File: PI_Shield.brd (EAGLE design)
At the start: 153.7 x 84.8 mm, 64 parts, among them Q1 220mA/50V/3.5Ω, Q3 220mA/50V/3.5Ω, Q4 220mA/50V/3.5Ω, Q5 2.5A/30V/105mΩ, U1 MAX1136EUA-T, U2 AZ1117EH-3.3TRG1, Y1 ECS-80-S-4X

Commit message: Update PI_Shield.brd
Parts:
- moved C11 191.3 mm to (49.5, -21.6)
- moved C12 191.3 mm to (45.7, -21.6)
- moved C13 191.3 mm to (41.9, -21.6)
- moved C3 191.3 mm to (72.4, -21.6)
- moved C4 191.3 mm to (68.6, -21.6)
- moved C5 191.3 mm to (64.8, -21.6)
- moved C6 191.3 mm to (61.0, -21.6)
- moved C8 191.3 mm to (57.1, -21.6)
- moved C9 191.3 mm to (53.3, -21.6)
- moved D1 191.3 mm to (77.5, -21.6)
- moved D2 191.3 mm to (68.6, -17.8)
- moved D4 191.3 mm to (64.8, -17.8)
- moved R1 191.3 mm to (38.1, -21.6)
- moved R10 191.3 mm to (99.1, -16.5)
- moved R11 191.3 mm to (82.5, -21.6)
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
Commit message: Update PI_Shield.brd
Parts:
- moved C4 13.1 mm to (74.9, -10.2)
- moved C5 13.1 mm to (71.1, -10.2)
- moved D2 13.1 mm to (74.9, -6.35)
- moved D4 13.1 mm to (71.1, -6.35)
- moved R11 13.1 mm to (88.9, -10.2)
- moved R13 13.1 mm to (97.8, -5.08)
- moved R14 13.1 mm to (94.0, -5.08)
- moved R15 13.1 mm to (90.2, -5.08)
- moved R4 13.1 mm to (128.3, -5.08)
- moved R6 13.1 mm to (120.7, -5.08)
- moved R7 13.1 mm to (116.8, -5.08)
- moved C11 13.1 mm to (55.9, -10.2)
- moved C12 13.1 mm to (52.1, -10.2)
- moved C13 13.1 mm to (48.3, -10.2)
- moved C6 13.1 mm to (67.3, -10.2)
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
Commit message: Update PI_Shield.brd
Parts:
- moved R4 90.8 mm to (43.2, 26.7), turned to 90 degrees
- moved R5 83.7 mm to (47.0, 26.7), turned to 90 degrees
- moved C12 83.0 mm to (43.2, 72.4)
- moved 0 76.3 mm to (68.6, 62.2)
- moved R10 75.5 mm to (49.5, 45.7), turned to 90 degrees
- moved R12 73.5 mm to (31.8, 17.8), turned to 90 degrees
- moved C11 72.3 mm to (33.0, 58.4)
- moved R11 70.3 mm to (68.6, 57.1)
- moved R14 70.1 mm to (36.8, 35.6), turned to 270 degrees
- moved R15 69.1 mm to (31.8, 31.8), turned to 180 degrees
- moved C3 68.7 mm to (49.5, 52.1), turned to 270 degrees
- moved R13 67.1 mm to (36.8, 22.9), turned to 270 degrees
- moved R8 63.2 mm to (52.1, 11.4), turned to 90 degrees
- moved R2 62.0 mm to (64.8, 47.0), turned to 90 degrees
- moved D1 60.4 mm to (61.0, 45.7), turned to 270 degrees
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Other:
- board size 153.7 x 84.8 mm -> 85.1 x 84.8 mm

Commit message: Update PI_Shield.brd
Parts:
- moved U$8 33.3 mm to (36.8, 47.0)
- moved U2 27.4 mm to (43.2, 40.6)
- moved J4 23.3 mm to (33.0, 59.7), flipped to the bottom, turned to 270 degrees
- moved C11 17.8 mm to (33.0, 40.6)
- moved U$14 17.8 mm to (33.0, 69.8), turned to 0 degrees
- moved C12 16.5 mm to (49.5, 57.1)
- moved H1 15.5 mm to (86.4, 73.7)
- moved U$10 13.7 mm to (77.5, 16.5)
- moved U$13 13.7 mm to (77.5, 35.6)
- moved J2 11.7 mm to (81.3, 31.8)
- moved R6 11.7 mm to (64.8, 19.1)
- moved R20 11.5 mm to (86.4, 36.8), turned to 90 degrees
- moved J8 10.2 mm to (17.8, 58.4), turned to 270 degrees
- moved U$12 10.2 mm to (83.8, 50.8)
- moved U$9 10.2 mm to (83.8, 43.2)
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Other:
- board size 85.1 x 84.8 mm -> 85.1 x 72.1 mm

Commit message: wires setup
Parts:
- moved U$1 3.59 mm to (61.0, 63.5)
- moved C12 2.84 mm to (47.0, 55.9)
- moved C3 2.54 mm to (47.0, 52.1)
- moved R6 1.80 mm to (63.5, 20.3), turned to 180 degrees
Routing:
- net 3V3: track 0.00 -> 167.4 mm
- net SDA: track 0.00 -> 93.6 mm
- net 5V: track 0.00 -> 91.8 mm
- net SCL: track 0.00 -> 63.7 mm
- net CANH: track 0.00 -> 53.2 mm
- net DI1: track 0.00 -> 43.7 mm
- net DI2: track 0.00 -> 35.6 mm
- net CLK: track 0.00 -> 33.1 mm
- net DI3: track 0.00 -> 28.0 mm
- net INT: track 0.00 -> 23.5 mm
- net MISO: track 0.00 -> 20.6 mm
- net MOSI: track 0.00 -> 20.1 mm
- net CANL: track 0.00 -> 16.3 mm
- net N$9: track 0.00 -> 16.0 mm
- net SCL_ADC: track 0.00 -> 15.5 mm
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- added copper zone on layer 1, net GND

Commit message: Finished the wiring
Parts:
- moved U$11 15.7 mm to (33.0, 43.2), turned to 0 degrees
- moved H1 5.24 mm to (85.1, 68.6)
- moved J2 5.08 mm to (81.3, 26.7), turned to 90 degrees
- moved J6 3.59 mm to (86.4, 25.4)
- moved C11 2.84 mm to (35.6, 39.4)
- moved J8 2.84 mm to (19.1, 55.9)
- moved C9 2.84 mm to (39.4, 30.5), turned to 0 degrees
- moved R3 1.80 mm to (58.4, 30.5), turned to 90 degrees
- moved J1 1.27 mm to (81.3, 21.6)
- flipped C13 to the bottom
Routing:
- net 3V3: track 167.4 -> 266.8 mm, vias 0 -> 3
- net CANL: track 16.3 -> 85.3 mm, vias 0 -> 3
- net DI: track 9.24 -> 76.3 mm, vias 0 -> 2
- net PWM: track 0.00 -> 62.6 mm
- net SCL: track 63.7 -> 122.1 mm
- net 5V: track 91.8 -> 144.9 mm
- net AIN2: track 0.00 -> 47.0 mm, vias 0 -> 1
- net IMU_RESET: track 0.00 -> 40.9 mm
- net TXCAN: track 0.00 -> 36.9 mm, vias 0 -> 6
- net TX: track 0.00 -> 32.1 mm
- net RXCAN: track 0.00 -> 31.3 mm, vias 0 -> 4
- net CS: track 0.00 -> 31.0 mm, vias 0 -> 2
- net RESET_TO_PI: track 0.00 -> 29.1 mm, vias 0 -> 1
- net RX: track 0.00 -> 26.8 mm
- net IMU_INT: track 0.00 -> 26.6 mm
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
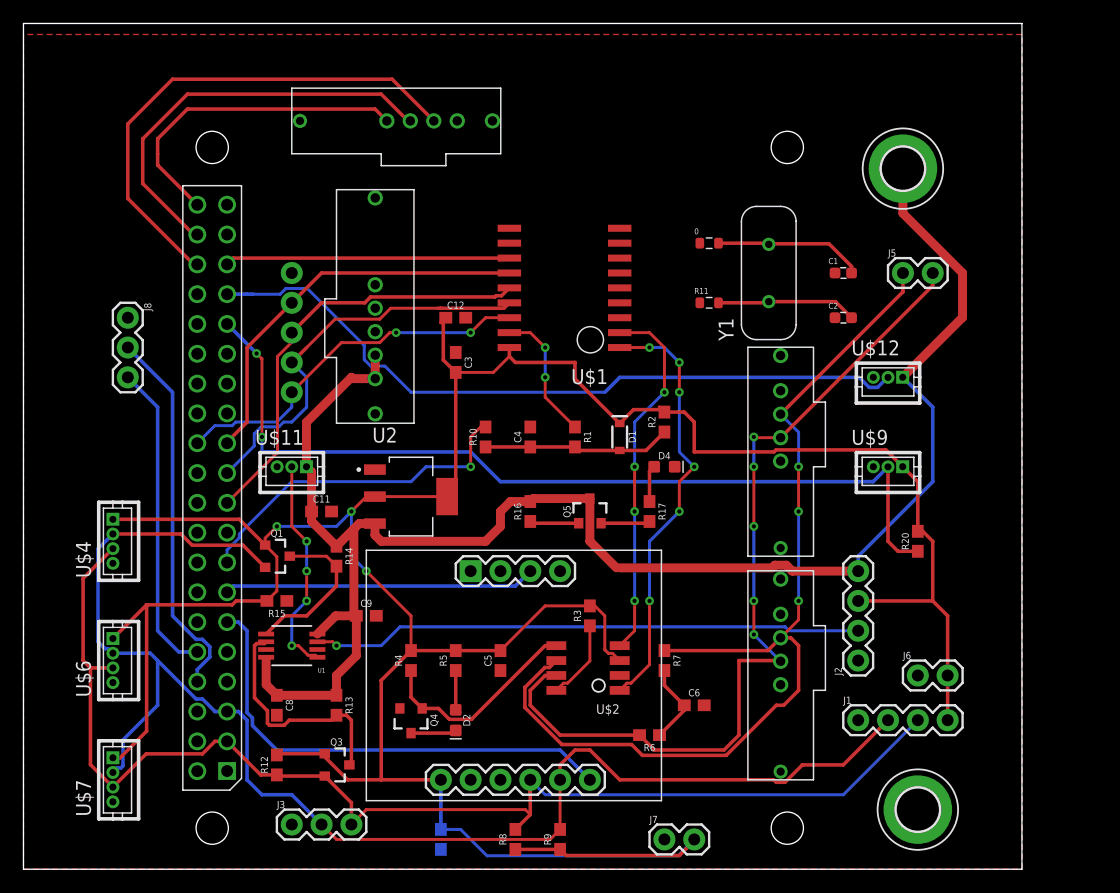
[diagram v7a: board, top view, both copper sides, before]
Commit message: fixed some errors
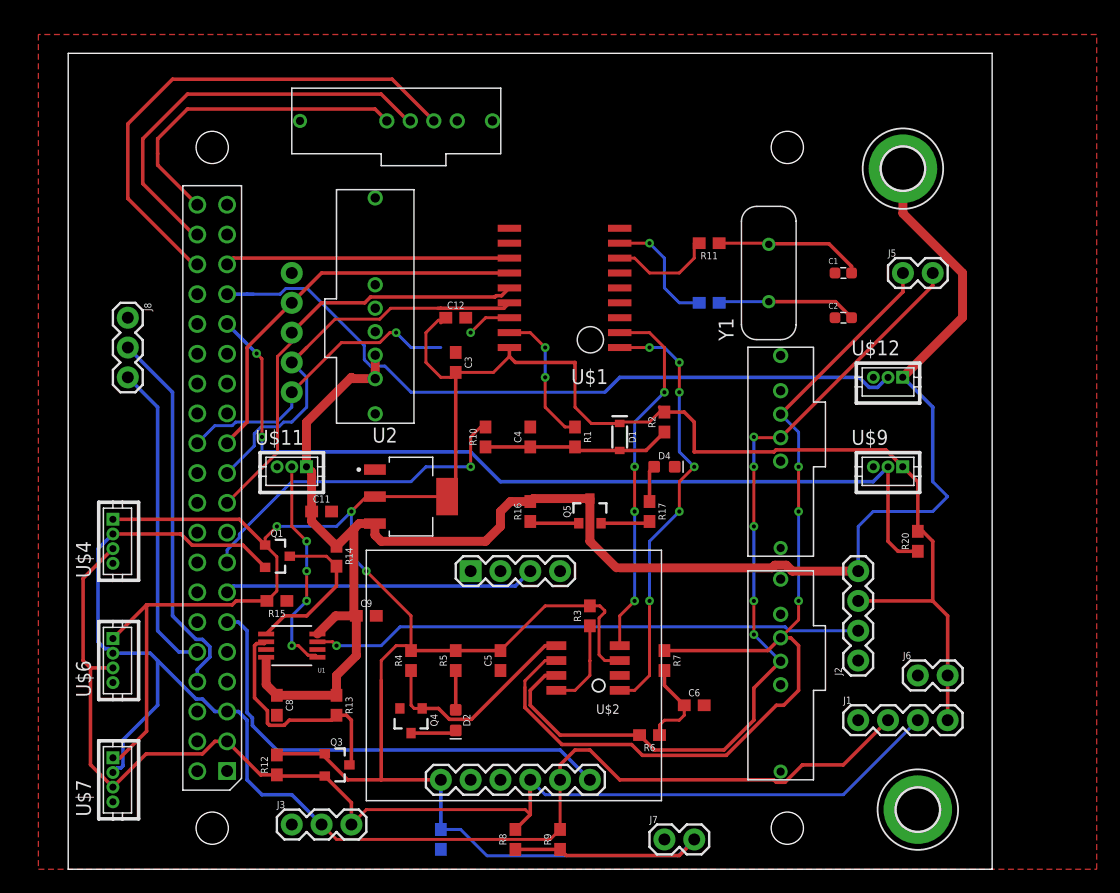
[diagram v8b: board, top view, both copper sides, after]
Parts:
- removed 0: R11, Resistor_Capacitor:RES_0603
- added R19: 0, SparkFun-Resistors:0603
- R11: device Resistor_Capacitor:RES_0603 -> SparkFun-Resistors:0603
- moved R11 5.08 mm to (68.6, 62.2), turned to 180 degrees
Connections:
- removed net N$4: 0.1
- removed net N$5: R11.1
- net N$2: now also R11.1; no longer 0.2
- net N$3: now also R19.1; no longer R11.2
- net OSC1: now also R19.2
- net OSC2: now also R11.2
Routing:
- net OSC1: track 0.00 -> 10.4 mm, vias 0 -> 1
- net OSC2: track 0.00 -> 9.09 mm
- net 3V3: track 266.8 -> 274.2 mm
- net 5V: track 144.9 -> 148.9 mm
- net CANH: track 75.6 -> 73.4 mm
- net CS: track 31.0 -> 29.0 mm
- net N$6: track 7.07 -> 8.25 mm
- net N$1: track 6.89 -> 7.62 mm
- net TXCAN: track 36.9 -> 37.4 mm
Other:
- board size 85.1 x 72.1 mm -> 78.7 x 69.5 mm
